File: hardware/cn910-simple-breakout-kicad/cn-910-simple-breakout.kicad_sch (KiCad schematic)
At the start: 9 parts, among them J1 CN910_FPC_CON, J2 J_PB_RF, J3 J_REC_RF

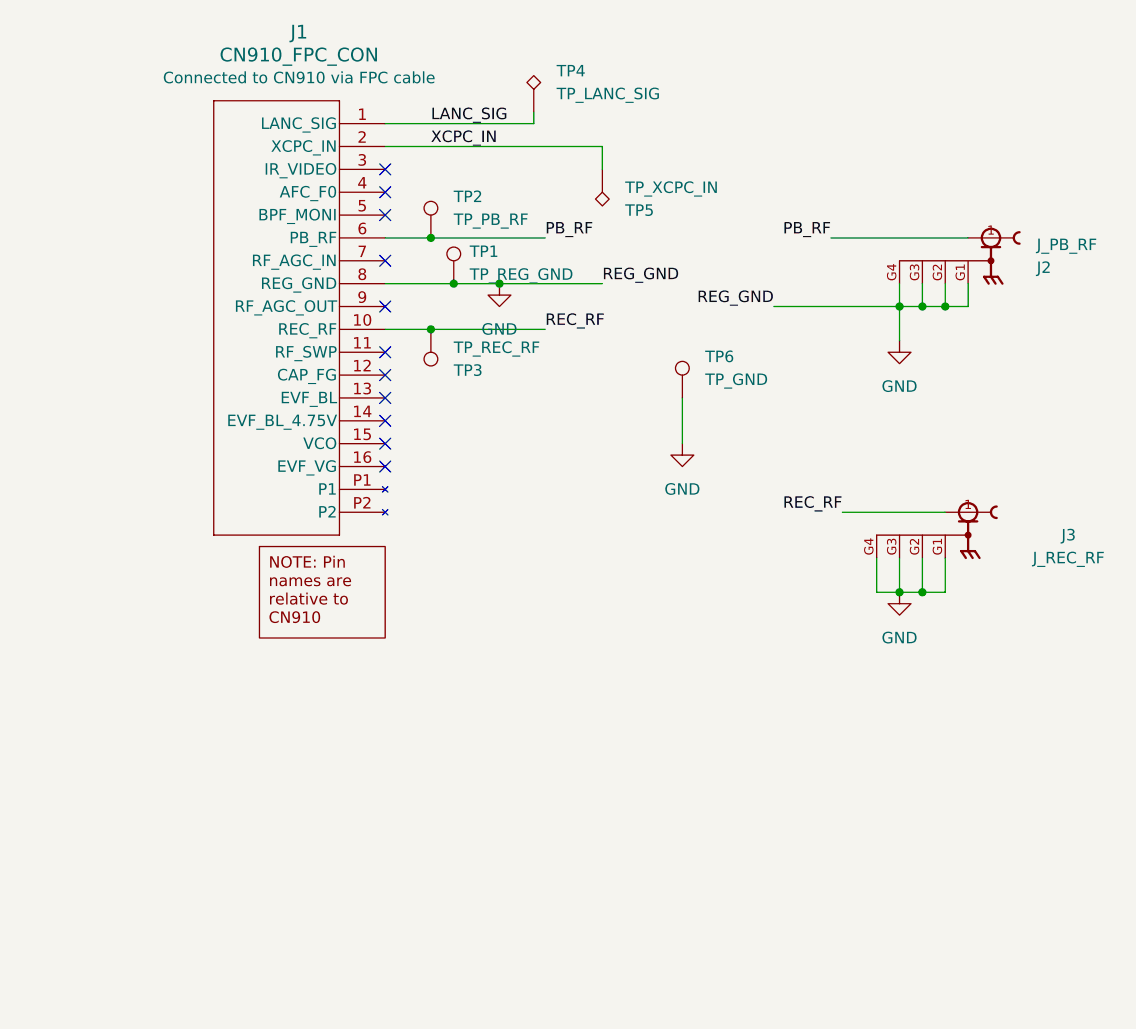
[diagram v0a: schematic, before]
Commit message: Enhanced CN910 breakout KiCad project with updated design rules, added new components, and refined PCB layout. Introduced a new simple breakout PCB with detailed Gerber files for manufacturing. Updated project metadata and library references for improved organization.
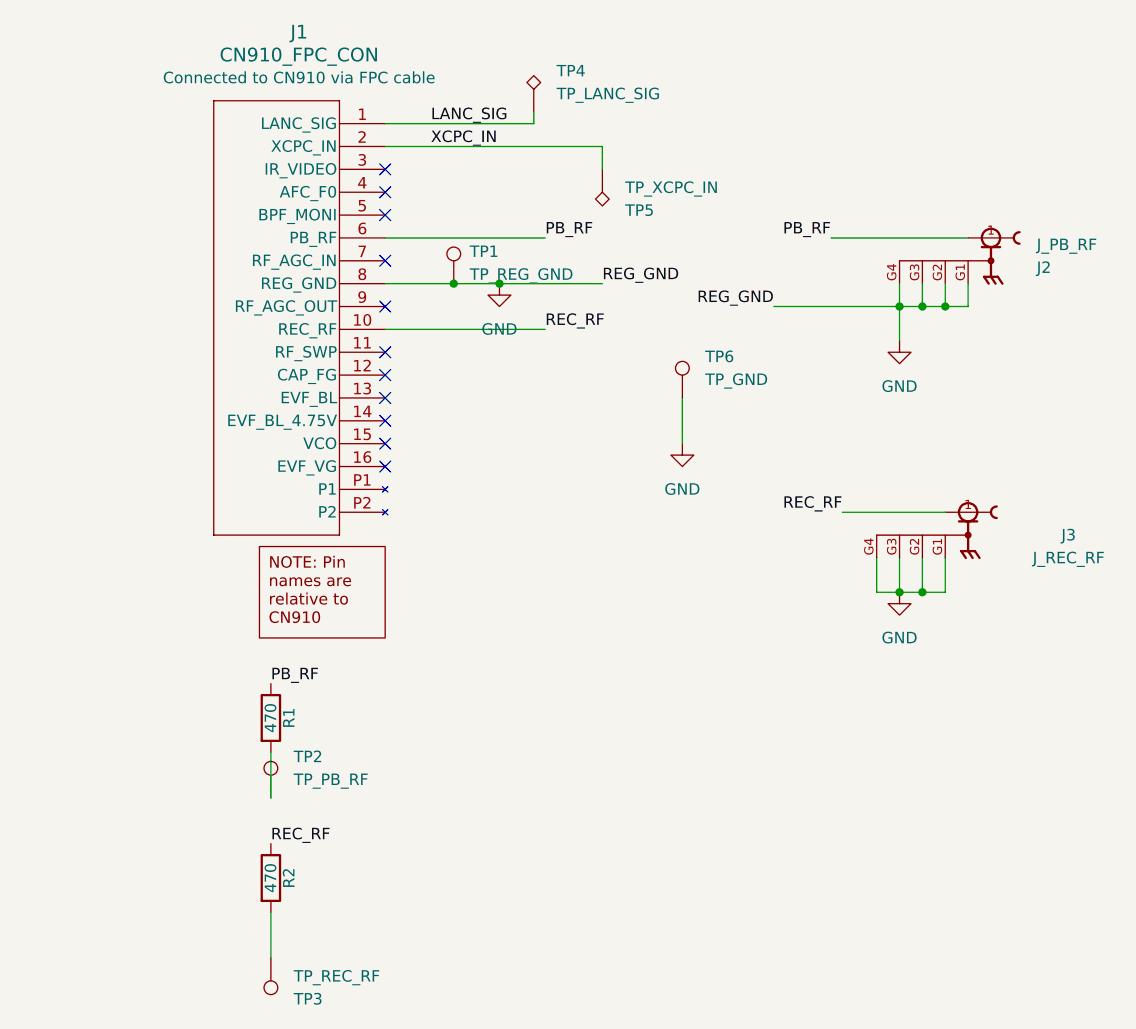
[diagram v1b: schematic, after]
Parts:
- added R1, R2: 470, Resistor_SMD:R_0603_1608Metric, symbol Device:R
- TP2, TP3: footprint TestPoint:TestPoint_Loop_D2.50mm_Drill1.0mm -> TestPoint:TestPoint_Pad_1.5x1.5mm
- TP6: footprint (none) -> TestPoint:TestPoint_Loop_D2.50mm_Drill1.0mm
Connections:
- net PB_RF: now also R1.1; no longer TP2.1
- net REC_RF: now also R2.1; no longer TP3.1
- new net: R1.2, TP2.1
- new net: R2.2, TP3.1
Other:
- moved on the sheet: TP2, TP3

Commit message: Refactored CN910 breakout KiCad project files, updating footprint and symbol references to "GDH" naming convention. Adjusted PCB thickness and dielectric properties for improved design accuracy. Added new adhesive layers and updated project metadata with a new variant description. Removed obsolete libraries and 3D models to streamline the project.
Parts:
- J1: footprint CN910:CON_527461671_MOL -> GDH Connectors:CON_527461671_MOL; symbol CN910:CN910_FPC_CON -> GDH Connectors:CN910_FPC_CON
- J2, J3: footprint CN910:GRADCONN_RFPC-SMA28-F -> GDH Connectors:GRADCONN_RFPC-SMA28-F; symbol CN910:RFPC-SMA28-F -> GDH Connectors:RFPC-SMA28-F

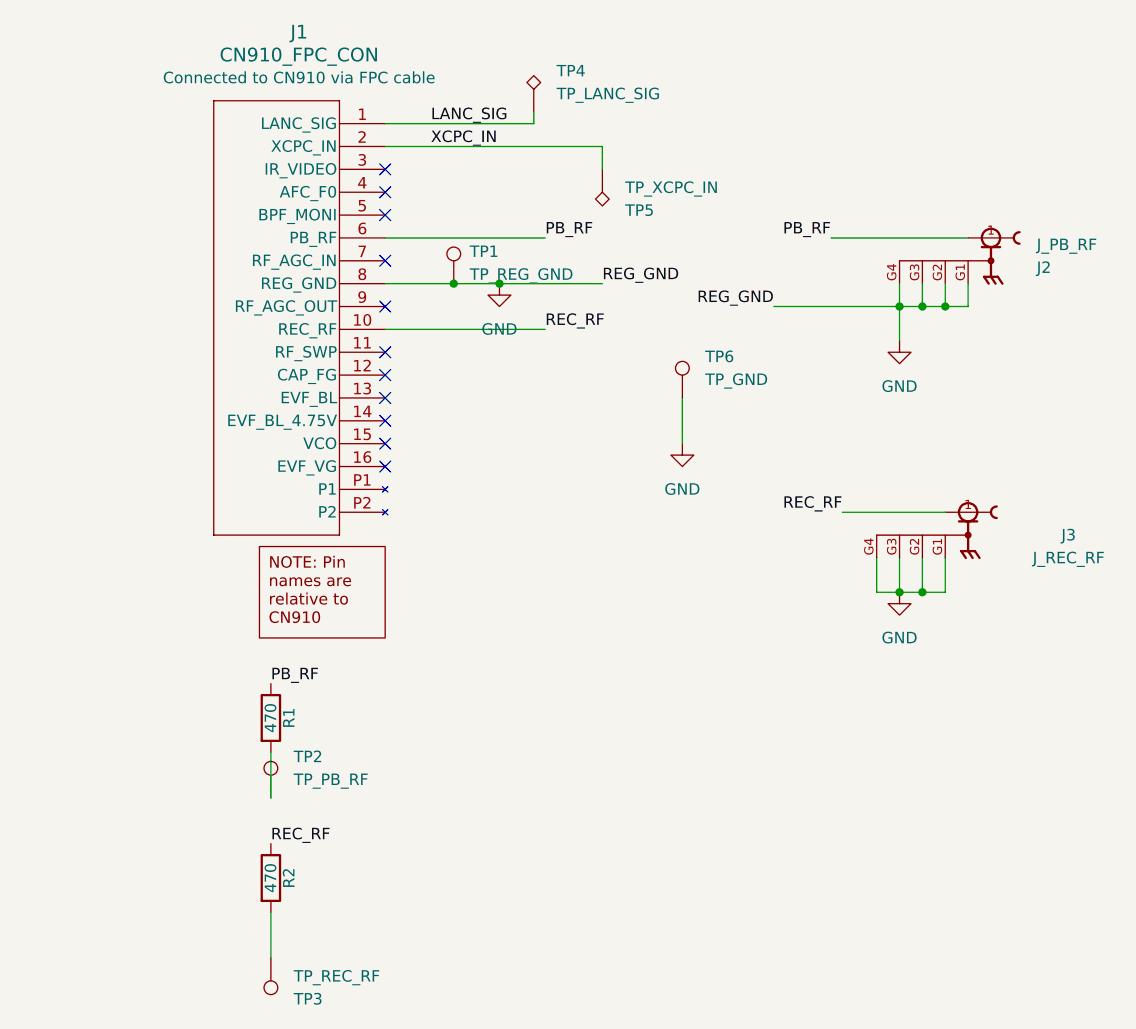
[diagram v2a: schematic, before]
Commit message: Updated CN910 breakout KiCad project files with dynamic project metadata, including title, company, version, and license. Refined design rules and component properties for improved clarity and organization. Adjusted pin functions and descriptions for connectors, and removed obsolete library references. Enhanced layout with new wire connections and updated schematic components.
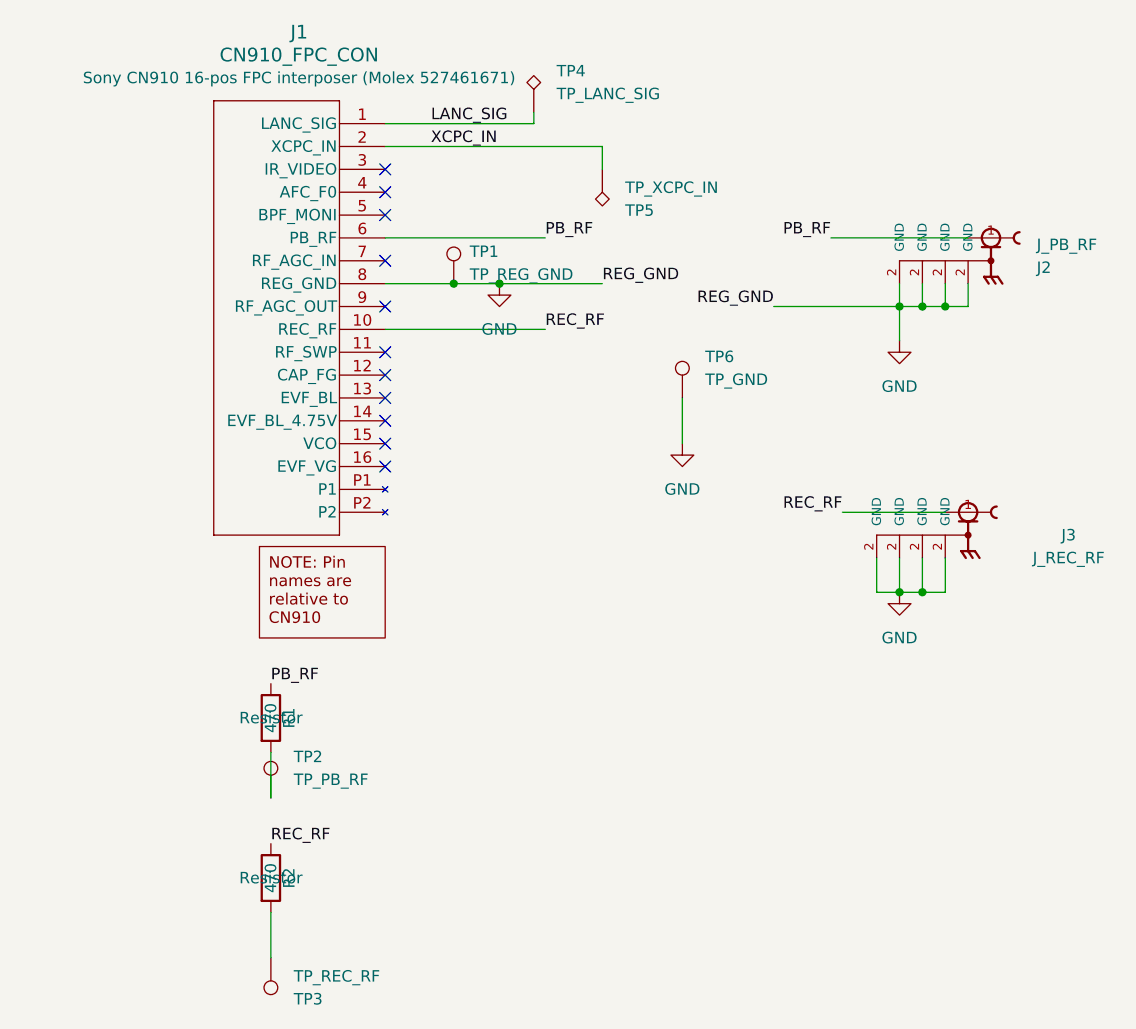
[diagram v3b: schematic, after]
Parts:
- J1: MPN (none) -> 527461671; Manufacturer (none) -> Molex
- J2, J3: MPN (none) -> RFPC-SMA28-F; Manufacturer (none) -> GCT
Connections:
- net GND: now also J2.2 (GND), J3.2 (GND); no longer J2.G1, J2.G2, J2.G3, J2.G4, J3.G1, J3.G2, J3.G3, J3.G4

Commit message: Updated CN910 breakout KiCad project files to reflect JLCPCB manufacturing specifications, including revised design rules for track width, via dimensions, and hole clearances. Adjusted component properties and footprints for test points, ensuring accurate descriptions and tags. Enhanced project metadata with dynamic title and versioning, while streamlining schematic connections and layout for improved clarity.
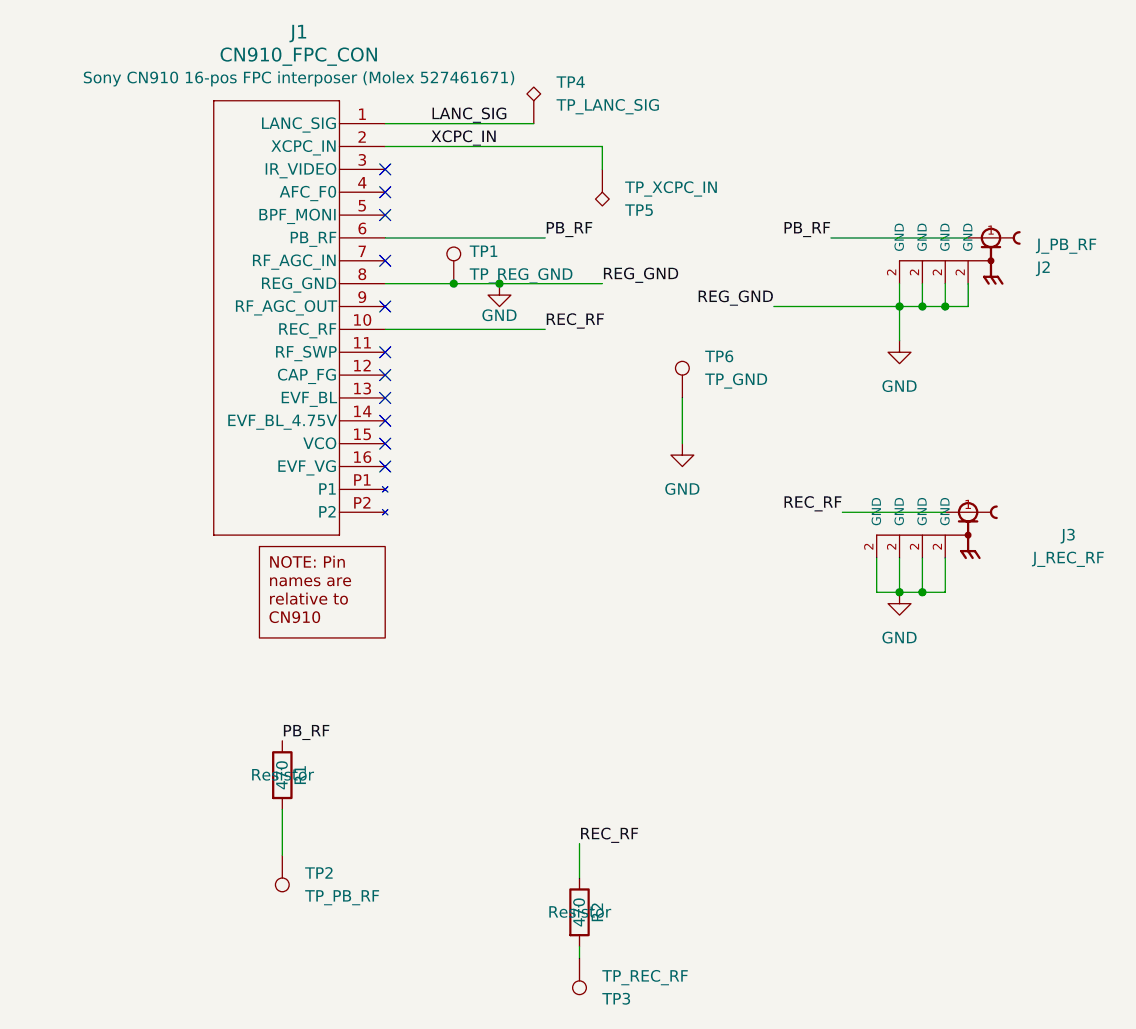
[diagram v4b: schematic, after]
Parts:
- TP2, TP3: footprint TestPoint:TestPoint_Pad_1.5x1.5mm -> TestPoint:TestPoint_Loop_D2.50mm_Drill1.0mm
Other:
- company: (none) -> ${proj-company}
- title: (none) -> ${proj-title}
- moved on the sheet: R1, R2, TP2, TP3, TP4
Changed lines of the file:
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@@
 	(generator_version "10.0")
 	(paper "A4")
+	(title_block
+		(title "${proj-title}")
+		(rev "${proj-version}")
+		(company "${proj-company}")
+	)
 	(junction
 		(at 148.59 110.49)
@@
 	(wire
 		(pts
+			(xy 139.7 101.6) (xy 151.13 101.6)
+		)
+		(stroke
+			(width 0)
+			(type default)
+		)
+	)
+	(wire
+		(pts
+			(xy 101.6 76.2) (xy 113.03 76.2)
+		)
+		(stroke
+			(width 0)
+			(type default)
+		)
+	)
+	(wire
+		(pts
+			(xy 121.92 93.98) (xy 121.92 88.9)
+		)
+		(stroke
+			(width 0)
+			(type default)
+		)
+	)
+	(wire
+		(pts
+			(xy 148.59 78.74) (xy 151.13 78.74)
+		)
+		(stroke
+			(width 0)
+			(type default)
+		)
+	)
+	(wire
+		(pts
+			(xy 151.13 78.74) (xy 153.67 78.74)
+		)
+		(stroke
+			(width 0)
+			(type default)
+		)
+	)
+	(wire
+		(pts
+			(xy 146.05 78.74) (xy 148.59 78.74)
+		)
+		(stroke
+			(width 0)
+			(type default)
+		)
+	)
+	(wire
+		(pts
+			(xy 143.51 106.68) (xy 143.51 110.49)
+		)
+		(stroke
+			(width 0)
+			(type default)
+		)
+	)
+	(wire
+		(pts
+			(xy 113.03 60.96) (xy 113.03 63.5)
+		)
+		(stroke
+			(width 0)
+			(type default)
+		)
+	)
+	(wire
+		(pts
 			(xy 138.43 71.12) (xy 153.67 71.12)
 		)
@@
 	(wire
 		(pts
-			(xy 139.7 101.6) (xy 151.13 101.6)
-		)
-		(stroke
-			(width 0)
-			(type default)
-		)
-	)
-	(wire
-		(pts
-			(xy 101.6 76.2) (xy 113.03 76.2)
-		)
-		(stroke
-			(width 0)
-			(type default)
-		)
-	)
-	(wire
-		(pts
-			(xy 121.92 93.98) (xy 121.92 88.9)
-		)
-		(stroke
-			(width 0)
-			(type default)
-		)
-	)
-	(wire
-		(pts
-			(xy 148.59 78.74) (xy 151.13 78.74)
-		)
-		(stroke
-			(width 0)
-			(type default)
-		)
-	)
-	(wire
-		(pts
-			(xy 105.41 58.42) (xy 105.41 57.15)
-		)
-		(stroke
-			(width 0)
-			(type default)
-		)
-	)
-	(wire
-		(pts
-			(xy 151.13 78.74) (xy 153.67 78.74)
-		)
-		(stroke
-			(width 0)
-			(type default)
-		)
-	)
-	(wire
-		(pts
-			(xy 146.05 78.74) (xy 148.59 78.74)
-		)
-		(stroke
-			(width 0)
-			(type default)
-		)
-	)
-	(wire
-		(pts
-			(xy 143.51 106.68) (xy 143.51 110.49)
-		)
-		(stroke
-			(width 0)
-			(type default)
-		)
-	)
-	(wire
-		(pts
-			(xy 113.03 60.96) (xy 113.03 63.5)
-		)
-		(stroke
-			(width 0)
-			(type default)
-		)
-	)
-	(wire
-		(pts
 			(xy 96.52 76.2) (xy 101.6 76.2)
 		)
@@
 	(wire
 		(pts
-			(xy 76.2 128.27) (xy 76.2 133.35)
+			(xy 77.47 134.62) (xy 77.47 139.7)
 		)
 		(stroke
@@
 	(wire
 		(pts
-			(xy 76.2 146.05) (xy 76.2 151.13)
+			(xy 110.49 149.86) (xy 110.49 151.13)
 		)
 		(stroke
@@
 		)
 	)
+	(wire
+		(pts
+			(xy 110.49 142.24) (xy 110.49 138.43)
+		)
+		(stroke
+			(width 0)
+			(type default)
+		)
+	)
 	(label "PB_RF"
-		(at 76.2 120.65 0)
+		(at 77.47 127 0)
 		(effects
 			(font
@@
 	)
 	(label "REC_RF"
-		(at 76.2 138.43 0)
+		(at 110.49 138.43 0)
 		(effects
 			(font
@@
 	(symbol
 		(lib_id "Device:R")
-		(at 76.2 124.46 0)
+		(at 77.47 130.81 0)
 		(unit 1)
 		(body_style 1)
@@
 		(dnp no)
 		(property "Reference" "R1"
-			(at 78.232 124.46 90)
+			(at 79.502 130.81 90)
 			(show_name no)
 			(do_not_autoplace no)
@@
 		)
 		(property "Value" "470"
-			(at 76.2 124.46 90)
+			(at 77.47 130.81 90)
 			(show_name no)
 			(do_not_autoplace no)
@@
 		)
 		(property "Footprint" "Resistor_SMD:R_0603_1608Metric"
-			(at 74.422 124.46 0)
+			(at 75.692 130.81 0)
 			(hide yes)
 			(show_name no)
@@
 		)
 		(property "Datasheet" "~"
-			(at 76.2 124.46 0)
+			(at 77.47 130.81 0)
 			(hide yes)
 			(show_name no)
@@
 		)
 		(property "Description" "Resistor"
-			(at 76.2 124.46 0)
+			(at 77.47 130.81 0)
 			(show_name no)
 			(do_not_autoplace no)
@@
 	(symbol
 		(lib_id "Connector:TestPoint")
-		(at 76.2 151.13 0)
+		(at 110.49 151.13 0)
 		(mirror x)
 		(unit 1)
@@
 		(dnp no)
 		(property "Reference" "TP3"
-			(at 78.74 155.7021 0)
+			(at 113.03 155.7021 0)
 			(show_name no)
 			(do_not_autoplace no)
@@
 		)
 		(property "Value" "TP_REC_RF"
-			(at 78.74 153.1621 0)
+			(at 113.03 153.1621 0)
 			(show_name no)
 			(do_not_autoplace no)
@@
 			)
 		)
-		(property "Footprint" "TestPoint:TestPoint_Pad_1.5x1.5mm"
-			(at 81.28 151.13 0)
+		(property "Footprint" "TestPoint:TestPoint_Loop_D2.50mm_Drill1.0mm"
+			(at 115.57 151.13 0)
 			(hide yes)
 			(show_name no)
@@
 		)
 		(property "Datasheet" ""
-			(at 81.28 151.13 0)
+			(at 115.57 151.13 0)
 			(hide yes)
 			(show_name no)
@@
 		)
 		(property "Description" "test point"
-			(at 76.2 151.13 0)
+			(at 110.49 151.13 0)
 			(hide yes)
 			(show_name no)
@@
 	(symbol
 		(lib_id "Device:R")
-		(at 76.2 142.24 0)
+		(at 110.49 146.05 0)
 		(unit 1)
 		(body_style 1)
@@
 		(dnp no)
 		(property "Reference" "R2"
-			(at 78.232 142.24 90)
+			(at 112.522 146.05 90)
 			(show_name no)
 			(do_not_autoplace no)
@@
 		)
 		(property "Value" "470"
-			(at 76.2 142.24 90)
+			(at 110.49 146.05 90)
 			(show_name no)
 			(do_not_autoplace no)
@@
 		)
 		(property "Footprint" "Resistor_SMD:R_0603_1608Metric"
-			(at 74.422 142.24 0)
+			(at 108.712 146.05 0)
 			(hide yes)
 			(show_name no)
@@
 		)
 		(property "Datasheet" "~"
-			(at 76.2 142.24 0)
+			(at 110.49 146.05 0)
 			(hide yes)
 			(show_name no)
@@
 		)
 		(property "Description" "Resistor"
-			(at 76.2 142.24 0)
+			(at 110.49 146.05 0)
 			(show_name no)
 			(do_not_autoplace no)
@@
 	(symbol
 		(lib_id "Connector:TestPoint_Alt")
-		(at 105.41 57.15 0)
+		(at 105.41 58.42 0)
 		(unit 1)
 		(body_style 1)
@@
 		(fields_autoplaced yes)
 		(property "Reference" "TP4"
-			(at 107.95 52.5779 0)
+			(at 107.95 53.8479 0)
 			(show_name no)
 			(do_not_autoplace no)
@@
 		)
 		(property "Value" "TP_LANC_SIG"
-			(at 107.95 55.1179 0)
+			(at 107.95 56.3879 0)
 			(show_name no)
 			(do_not_autoplace no)
@@
 		)
 		(property "Footprint" "TestPoint:TestPoint_Loop_D2.50mm_Drill1.0mm"
-			(at 110.49 57.15 0)
+			(at 110.49 58.42 0)
 			(hide yes)
 			(show_name no)
@@
 		)
 		(property "Datasheet" ""
-			(at 110.49 57.15 0)
+			(at 110.49 58.42 0)
 			(hide yes)
 			(show_name no)
@@
 		)
 		(property "Description" "test point (alternative shape)"
-			(at 105.41 57.15 0)
+			(at 105.41 58.42 0)
 			(hide yes)
 			(show_name no)
@@
 	(symbol
 		(lib_id "Connector:TestPoint")
-		(at 76.2 133.35 0)
+		(at 77.47 139.7 180)
 		(unit 1)
 		(body_style 1)
@@
 		(fields_autoplaced yes)
 		(property "Reference" "TP2"
-			(at 78.74 128.7779 0)
-			(show_name no)
-			(do_not_autoplace no)
-			(effects
-				(font
-					(size 1.27 1.27)
-				)
-				(justify left)
+			(at 80.01 141.7319 0)
+			(show_name no)
+			(do_not_autoplace no)
+			(effects
+				(font
+					(size 1.27 1.27)
+				)
+				(justify right)
 			)
 		)
 		(property "Value" "TP_PB_RF"
-			(at 78.74 131.3179 0)
-			(show_name no)
-			(do_not_autoplace no)
-			(effects
-				(font
-					(size 1.27 1.27)
-				)
-				(justify left)
-			)
-		)
-		(property "Footprint" "TestPoint:TestPoint_Pad_1.5x1.5mm"
-			(at 81.28 133.35 0)
+			(at 80.01 144.2719 0)
+			(show_name no)
+			(do_not_autoplace no)
+			(effects
+				(font
+					(size 1.27 1.27)
+				)
+				(justify right)
+			)
+		)
+		(property "Footprint" "TestPoint:TestPoint_Loop_D2.50mm_Drill1.0mm"
+			(at 72.39 139.7 0)
 			(hide yes)
 			(show_name no)
@@
 		)
 		(property "Datasheet" ""
-			(at 81.28 133.35 0)
+			(at 72.39 139.7 0)
 			(hide yes)
 			(show_name no)
@@
 		)
 		(property "Description" "test point"
-			(at 76.2 133.35 0)
+			(at 77.47 139.7 0)
 			(hide yes)
 			(show_name no)
@@
 		(in_pos_files yes)
 		(dnp no)
-		(fields_autoplaced yes)
 		(property "Reference" "#PWR03"
 			(at 101.6 82.55 0)
@@
 		)
 		(property "Value" "GND"
-			(at 101.6 81.28 0)
-			(show_name no)
-			(do_not_autoplace no)
+			(at 101.6 79.756 0)
+			(show_name no)
+			(do_not_autoplace no)
